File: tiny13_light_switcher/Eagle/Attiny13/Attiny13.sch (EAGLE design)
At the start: 39 parts, among them Q4 2N7000, Q5 2N7000, Q6 2N7000, U1 ATTiny13, U2 ATTiny85

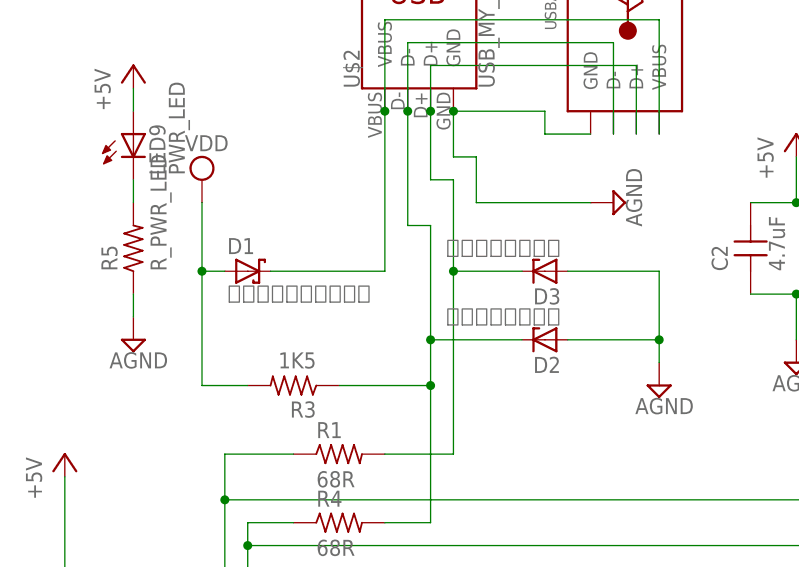
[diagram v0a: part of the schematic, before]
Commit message: Change PCB Size.
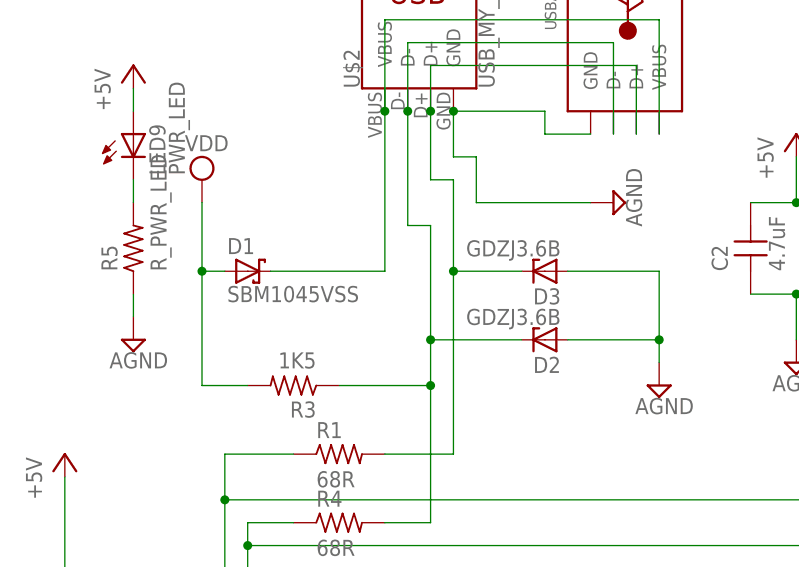
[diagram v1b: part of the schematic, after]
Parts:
- D1: value ＳＢＭ１０４５ＶＳＳ -> SBM1045VSS
- D2, D3: value ＧＤＺＪ３．６Ｂ -> GDZJ3.6B
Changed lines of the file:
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@@
 <part name="LED2" library="led" deviceset="LED" device="3MM" value="RED"/>
 <part name="U2" library="atmel" deviceset="TINY13*" device="8P3" value="ATTiny85"/>
-<part name="D1" library="adafruit" deviceset="SCHOTTKY-DIODE" device="DO41" value="ＳＢＭ１０４５ＶＳＳ"/>
-<part name="D2" library="diode" library_urn="urn:adsk.eagle:library:210" deviceset="ZENER-DIODE" device="DO34-7" value="ＧＤＺＪ３．６Ｂ"/>
-<part name="D3" library="diode" library_urn="urn:adsk.eagle:library:210" deviceset="ZENER-DIODE" device="DO34-7" value="ＧＤＺＪ３．６Ｂ"/>
+<part name="D1" library="adafruit" deviceset="SCHOTTKY-DIODE" device="DO41" value="SBM1045VSS"/>
+<part name="D2" library="diode" library_urn="urn:adsk.eagle:library:210" deviceset="ZENER-DIODE" device="DO34-7" value="GDZJ3.6B"/>
+<part name="D3" library="diode" library_urn="urn:adsk.eagle:library:210" deviceset="ZENER-DIODE" device="DO34-7" value="GDZJ3.6B"/>
 <part name="R1" library="MyLib" deviceset="R" device="0.125W_3P" value="68R"/>
 <part name="P+2" library="supply1" library_urn="urn:adsk.eagle:library:371" deviceset="+5V" device=""/>

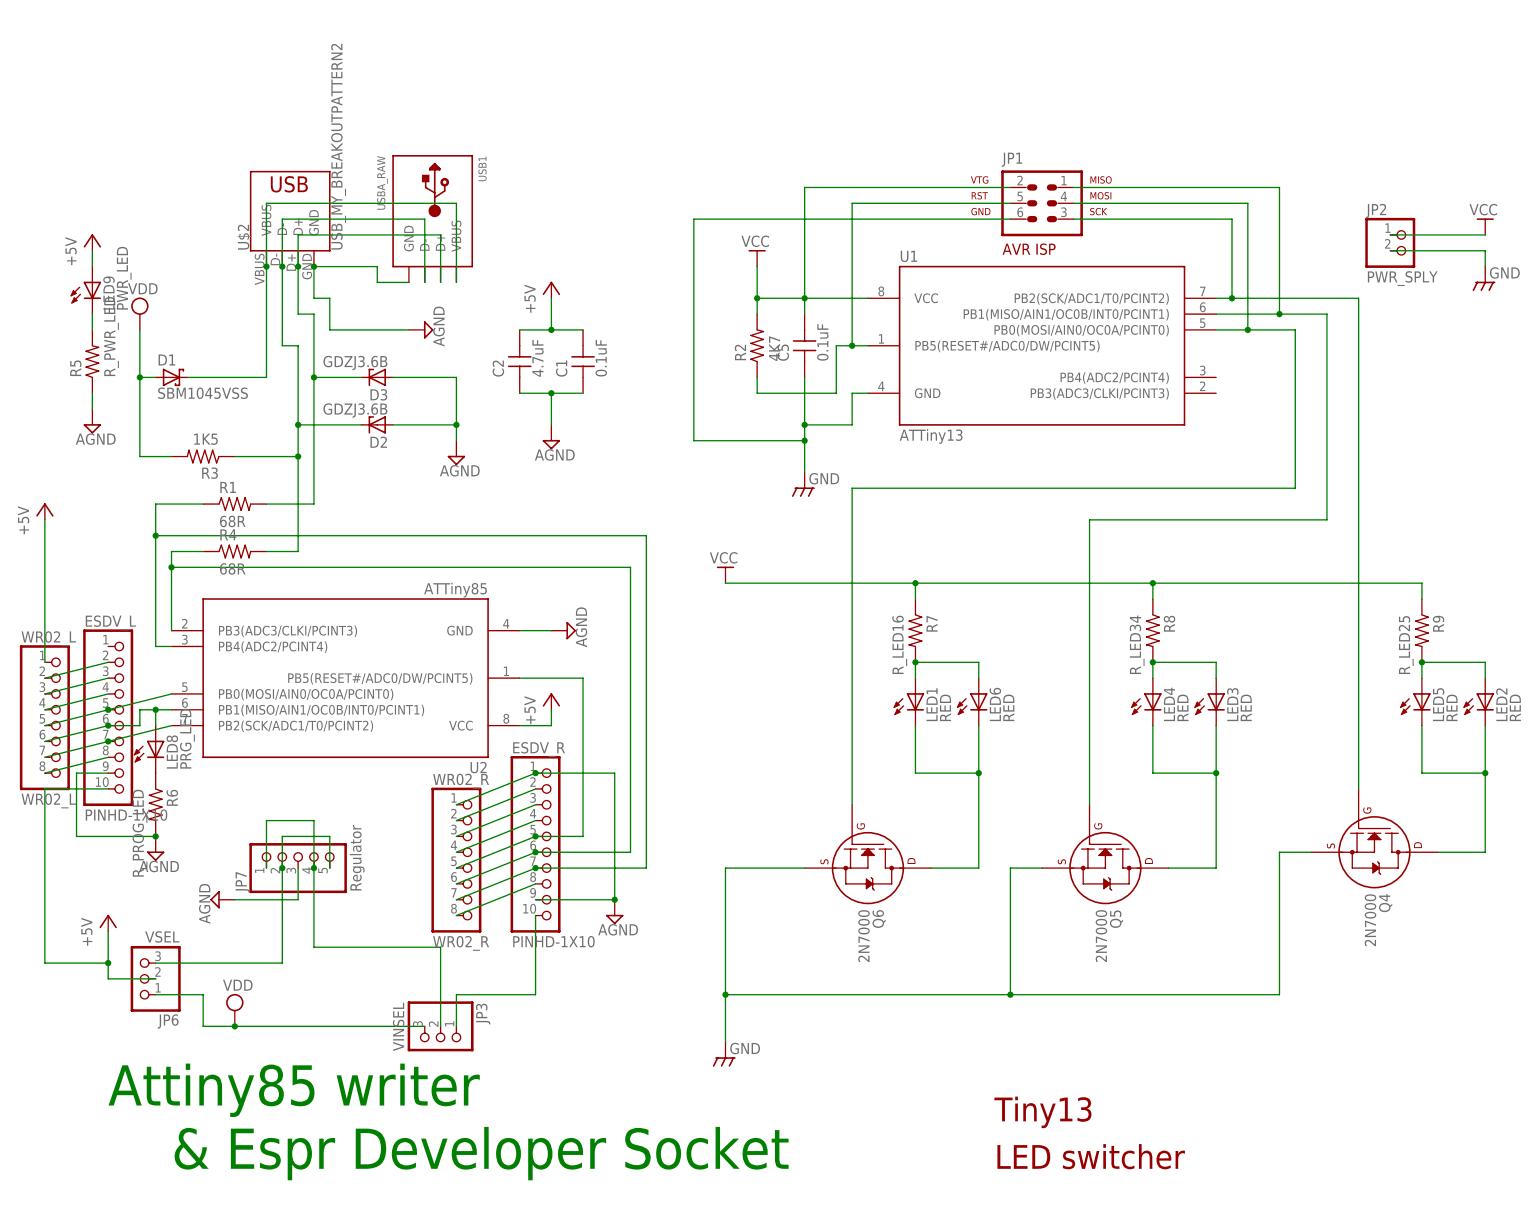
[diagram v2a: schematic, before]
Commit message: Spread Pin holes & Change LED Direction.
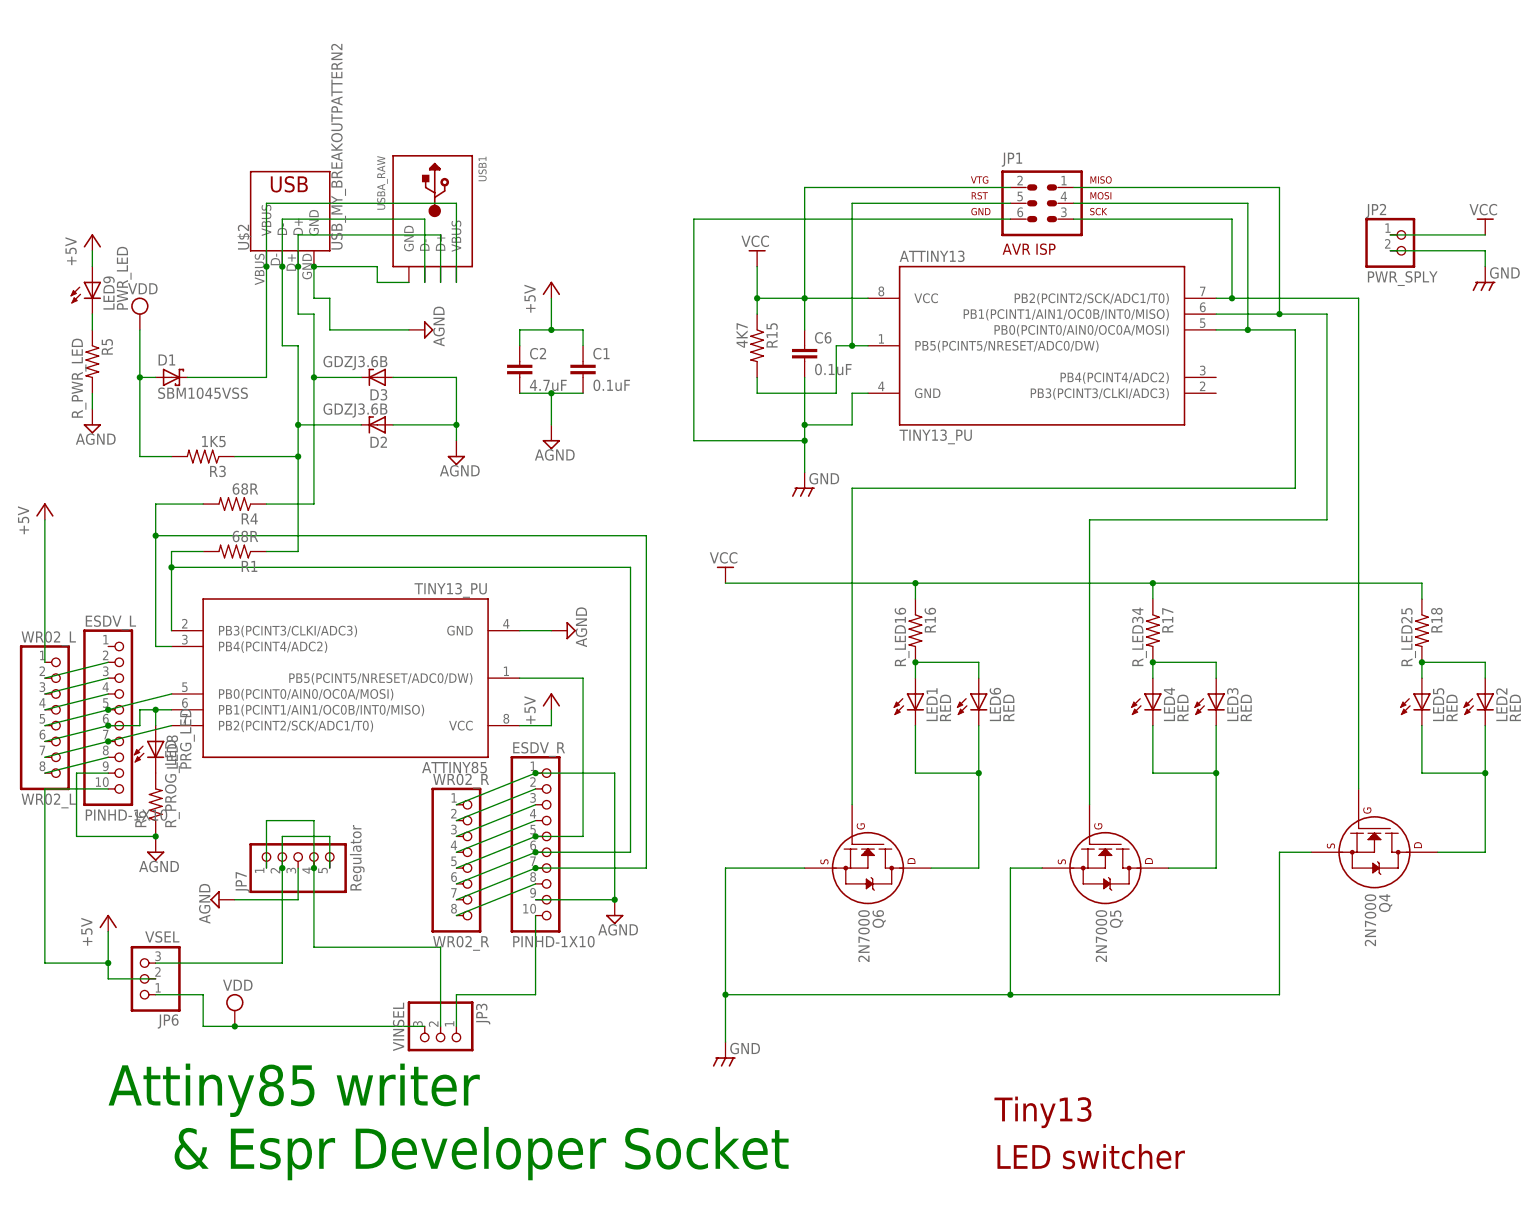
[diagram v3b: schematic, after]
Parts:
- removed C5: 0.1uF, MyLib:CAPDIP_2
- removed R2: 4K7, MyLib:R0.125W_3P
- removed R7: R_LED16, MyLib:R0.125W_3P
- removed R8: R_LED34, MyLib:R0.125W_3P
- removed R9: R_LED25, MyLib:R0.125W_3P
- removed U1: ATTiny13, atmel:TINY138P3
- removed U2: ATTiny85, atmel:TINY138P3
- added ATTINY13, ATTINY85: TINY13_PU, MyParts:TINY13_PU
- added C6: 0.1uF, resistor:C-EU050-025X075
- added R15: 4K7, resistor:R-US_0204/7
- added R16: R_LED16, resistor:R-US_0204/7
- added R17: R_LED34, resistor:R-US_0204/7
- added R18: R_LED25, resistor:R-US_0204/7
- C1, C2: device MyLib:CAPDIP_2 -> resistor:C-EU050-025X075
- LED1, LED2, LED3, LED4, LED5, LED6: device led:LED3MM -> led:LEDSFH480
- R1, R3, R4, R5, R6: device MyLib:R0.125W_3P -> resistor:R-US_0204/7
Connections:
- net +5V: now also ATTINY85.VCC, C1.1, C2.1; no longer C1.2, C2.2, U2.VCC
- net AGND: now also ATTINY85.GND, C1.2, C2.2, R5.2, R6.1; no longer C1.1, C2.1, R5.1, R6.2, U2.GND
- net GND: now also ATTINY13.GND, C6.2; no longer C5.1, U1.GND
- net N$11: now also ATTINY85.PB4(PCINT4/ADC2), R4.2; no longer R1.1, U2.PB4(ADC2/PCINT4)
- net N$12: now also ATTINY85.PB5(PCINT5/NRESET/ADC0/DW); no longer U2.PB5(RESET#/ADC0/DW/PCINT5)
- net N$13: now also R5.1; no longer R5.2
- net N$14: now also R6.2; no longer R6.1
- net N$15: now also ATTINY85.PB1(PCINT1/AIN1/OC0B/INT0/MISO); no longer U2.PB1(MISO/AIN1/OC0B/INT0/PCINT1)
- net N$16: now also ATTINY85.PB0(PCINT0/AIN0/OC0A/MOSI); no longer U2.PB0(MOSI/AIN0/OC0A/PCINT0)
- net N$18: now also ATTINY85.PB2(PCINT2/SCK/ADC1/T0); no longer U2.PB2(SCK/ADC1/T0/PCINT2)
- net N$19: now also R4.1; no longer R1.2
- net N$2: now also ATTINY13.PB2(PCINT2/SCK/ADC1/T0); no longer U1.PB2(SCK/ADC1/T0/PCINT2)
- net N$3: now also ATTINY85.PB3(PCINT3/CLKI/ADC3), R1.2; no longer R4.1, U2.PB3(ADC3/CLKI/PCINT3)
- net N$30: now also R16.2; no longer R7.2
- net N$31: now also R17.2; no longer R8.2
- net N$32: now also R18.2; no longer R9.2
- net N$4: now also R1.1; no longer R4.2
- net N$6: now also ATTINY13.PB0(PCINT0/AIN0/OC0A/MOSI); no longer U1.PB0(MOSI/AIN0/OC0A/PCINT0)
- net N$7: now also ATTINY13.PB5(PCINT5/NRESET/ADC0/DW), R15.2; no longer R2.1, U1.PB5(RESET#/ADC0/DW/PCINT5)
- net N$8: now also ATTINY13.PB1(PCINT1/AIN1/OC0B/INT0/MISO); no longer U1.PB1(MISO/AIN1/OC0B/INT0/PCINT1)
- net VCC: now also ATTINY13.VCC, C6.1, R15.1, R16.1, R17.1, R18.1; no longer C5.2, R2.2, R7.1, R8.1, R9.1, U1.VCC
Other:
- moved on the sheet: R1, R4, R5, R6
